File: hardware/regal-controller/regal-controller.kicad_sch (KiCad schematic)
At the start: 23 parts, among them J1 Raspberry_Pi_2_3, J2 Barrel_Jack_Switch_Pin3Ring, J3 Conn_02x05_Odd_Even, J4 Conn_01x02_Male, J5 Conn_01x02_Male, U1 SN65HVD230, U2 MCP2515, Y1 8MHz

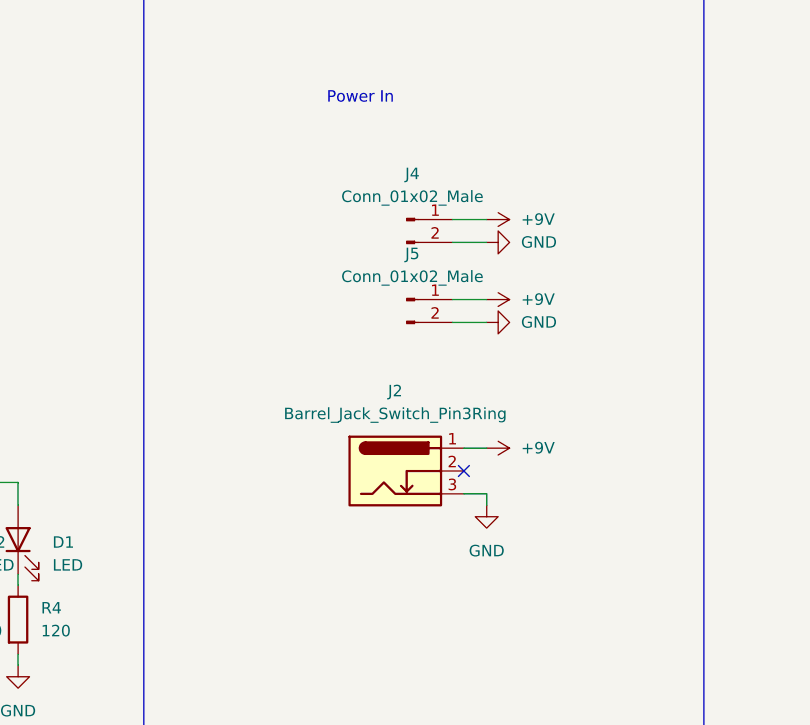
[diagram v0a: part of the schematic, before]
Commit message: 40pol connector rotated and other small mods.
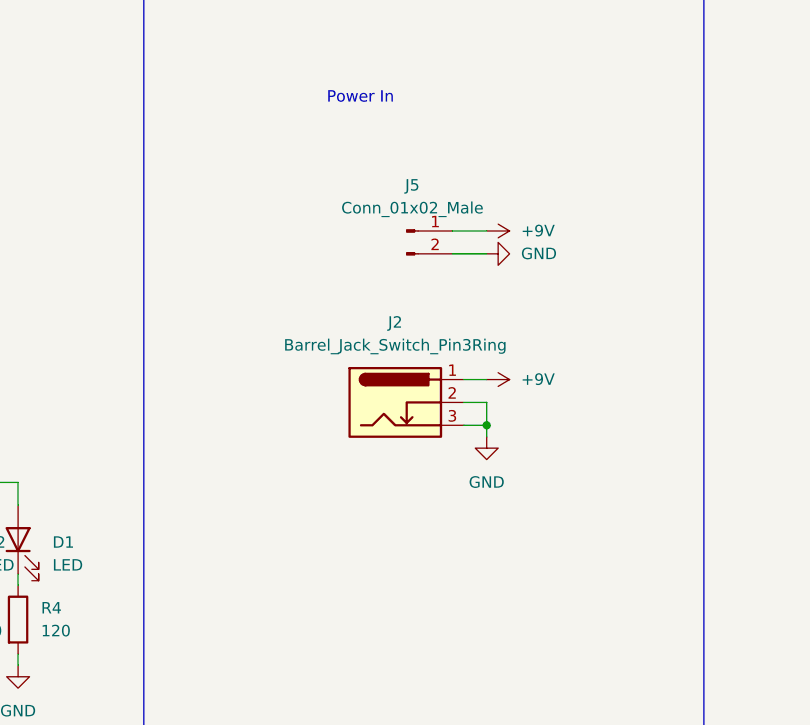
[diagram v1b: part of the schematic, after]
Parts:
- removed J4: Conn_01x02_Male, Connector_JST:JST_VH_B2PS-VH_1x02_P3.96mm_Horizontal, symbol Connector:Conn_01x02_Male
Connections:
- net GND: now also J2.2
- no-connect marks 36 -> 35
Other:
- moved on the sheet: J2, J5

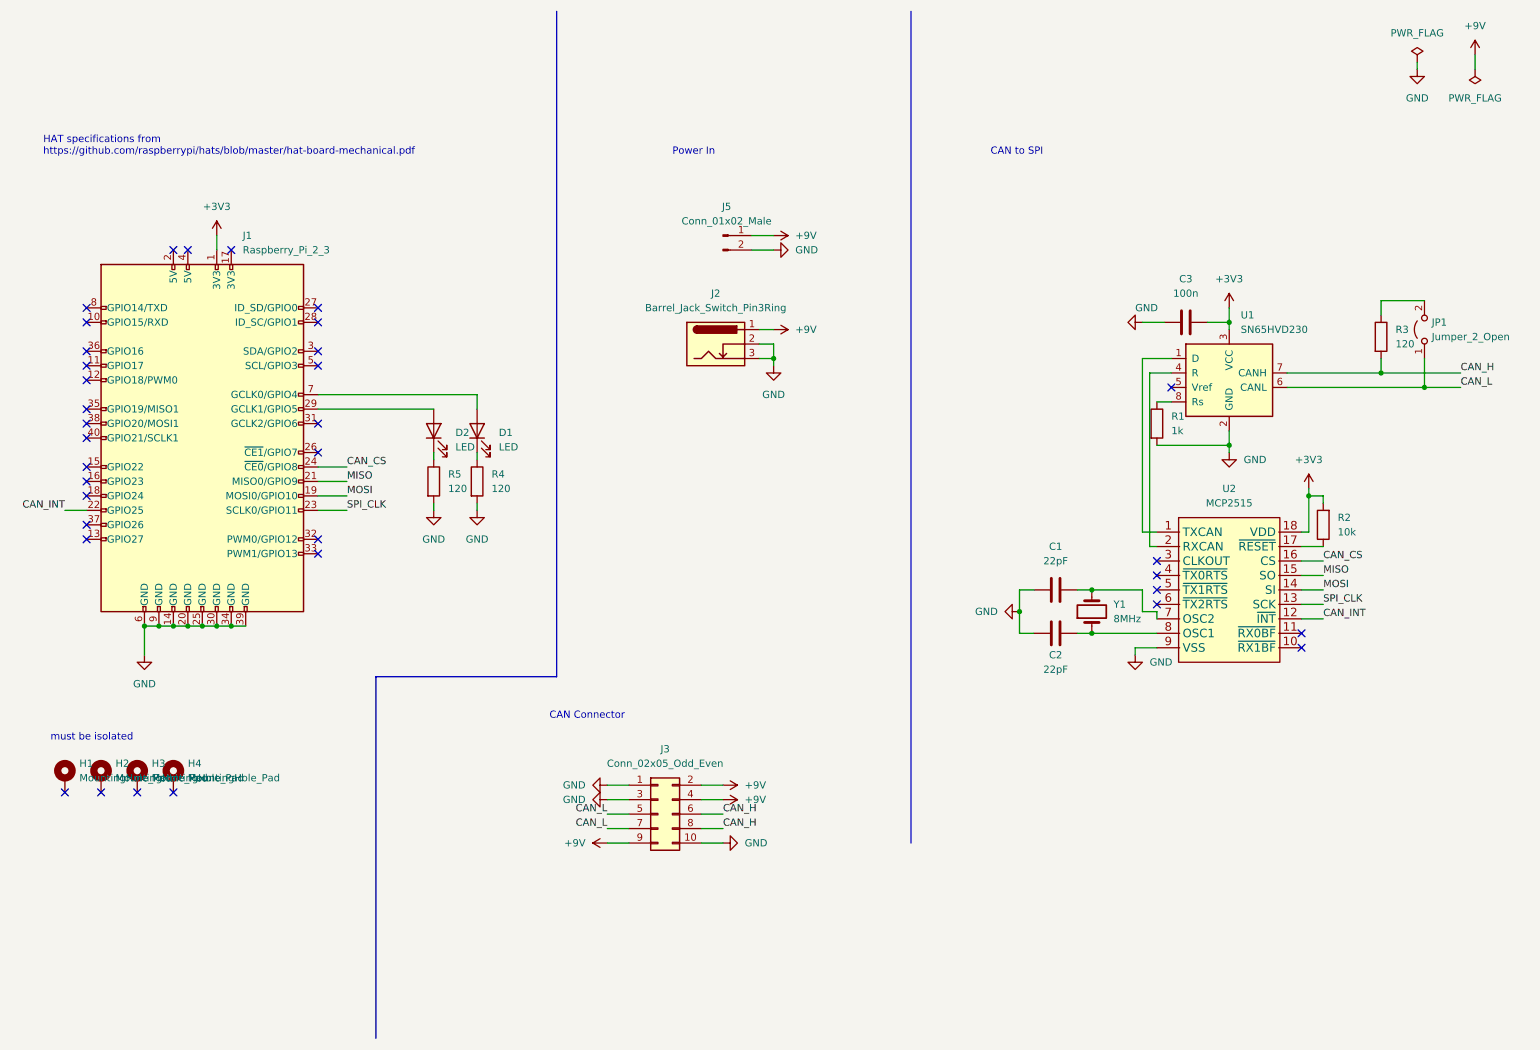
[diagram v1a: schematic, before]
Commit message: shelf controller USB added
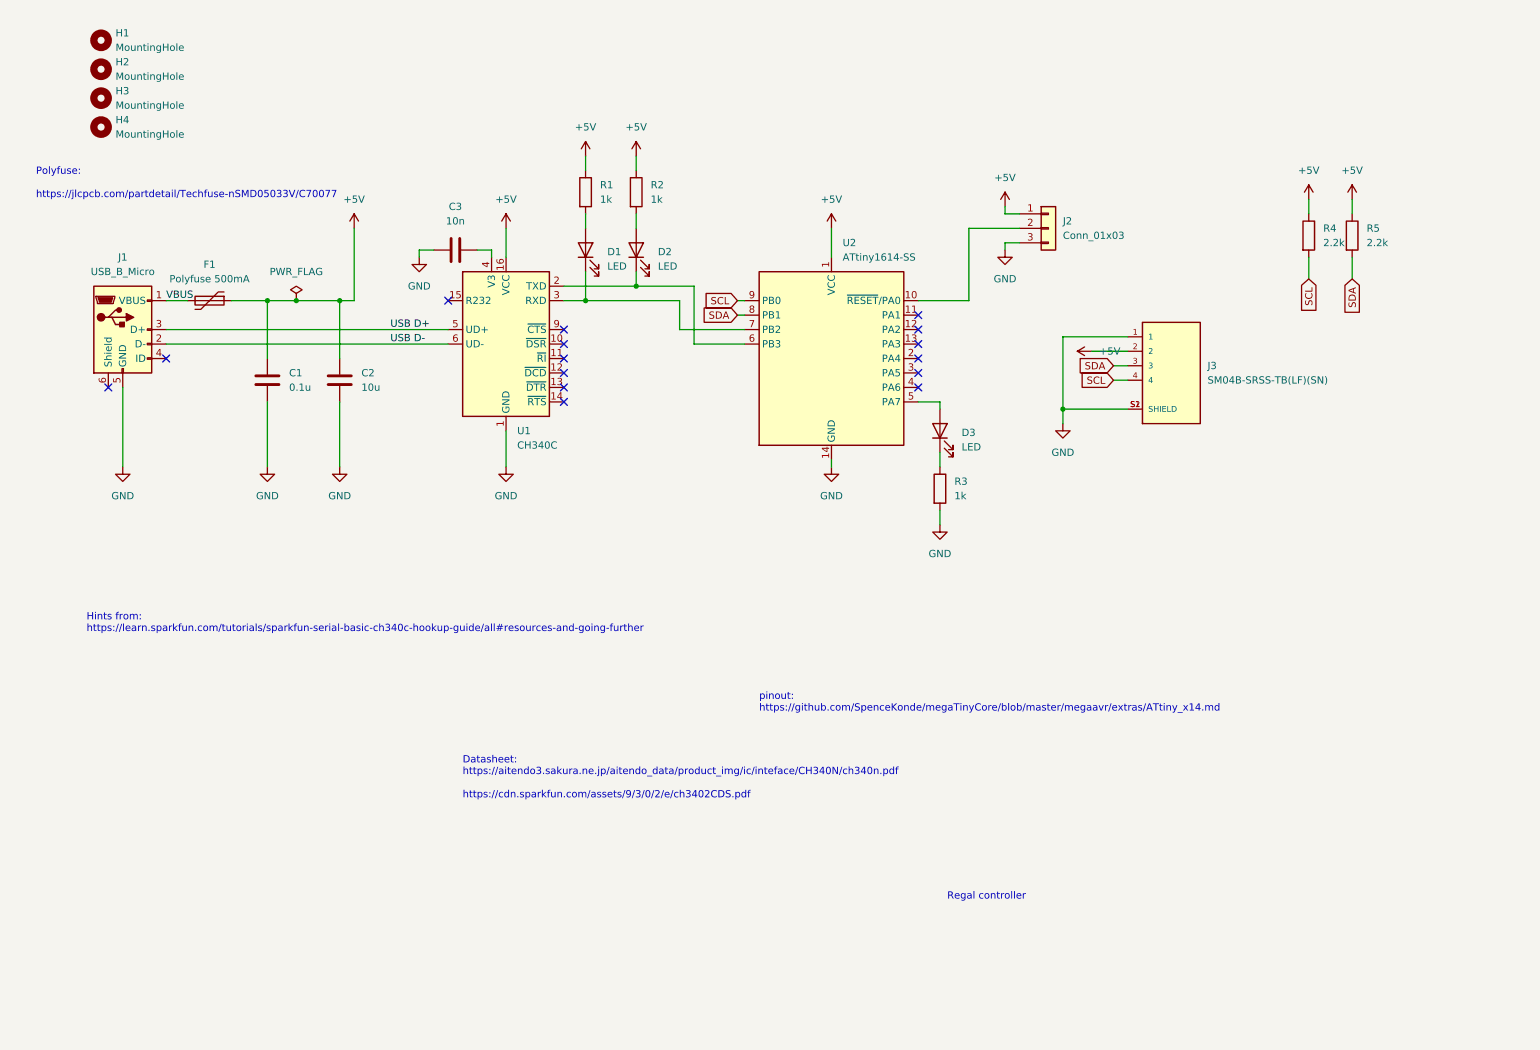
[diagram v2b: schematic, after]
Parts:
- removed H1, H2, H3, H4: MountingHole_Pad, MountingHole:MountingHole_2.7mm_M2.5_Pad_TopBottom, symbol Mechanical:MountingHole_Pad
- removed J1: Raspberry_Pi_2_3, Connector_PinSocket_2.54mm:PinSocket_2x20_P2.54mm_Vertical, symbol Connector:Raspberry_Pi_2_3
- removed J2: Barrel_Jack_Switch_Pin3Ring, Connector_BarrelJack:BarrelJack_Horizontal, symbol Connector:Barrel_Jack_Switch_Pin3Ring
- removed J3: Conn_02x05_Odd_Even, Connector_PinSocket_2.54mm:PinSocket_2x05_P2.54mm_Horizontal, symbol Connector_Generic:Conn_02x05_Odd_Even
- removed J5: Conn_01x02_Male, Connector_PinHeader_2.54mm:PinHeader_1x02_P2.54mm_Vertical, symbol Connector:Conn_01x02_Male
- removed JP1: Jumper_2_Open, TestPoint:TestPoint_2Pads_Pitch2.54mm_Drill0.8mm, symbol Jumper:Jumper_2_Open
- removed U1: SN65HVD230, Package_SO:SOIC-8_3.9x4.9mm_P1.27mm, symbol Interface_CAN_LIN:SN65HVD230
- removed U2: MCP2515, Package_DIP:DIP-18_W7.62mm_LongPads, symbol MCP2515:MCP2515
- removed Y1: 8MHz, Crystal:Crystal_SMD_HC49-SD_HandSoldering, symbol Device:Crystal
- added D3: LED, LED_SMD:LED_1206_3216Metric, symbol Device:LED
- added F1: Polyfuse 500mA, Fuse:Fuse_1206_3216Metric, symbol Device:Polyfuse
- added H1, H2, H3, H4: MountingHole, MountingHole:MountingHole_3.2mm_M3, symbol Mechanical:MountingHole
- added J1: USB_B_Micro, Connector_USB:USB_Micro-B_XKB_U254-051T-4BH83-F1S, symbol Connector:USB_B_Micro
- added J2: Conn_01x03, Connector_PinSocket_2.54mm:PinSocket_1x03_P2.54mm_Vertical, symbol Connector_Generic:Conn_01x03
- added J3: SM04B-SRSS-TB(LF)(SN), MyConnector:JST_SM04B-SRSS-TB(LF)(SN), symbol MyConnector:SM04B-SRSS-TB(LF)(SN)
- added U1: CH340C, Package_SO:SOIC-16_3.9x9.9mm_P1.27mm, symbol Interface_USB:CH340C
- added U2: ATtiny1614-SS, Package_SO:SOIC-14_3.9x8.7mm_P1.27mm, symbol MCU_Microchip_ATtiny:ATtiny1614-SS
- C1: value 22pF -> 0.1u; footprint Capacitor_SMD:C_1206_3216Metric_Pad1.33x1.80mm_HandSolder -> Capacitor_SMD:C_1206_3216Metric
- C2: value 22pF -> 10u; footprint Capacitor_SMD:C_1206_3216Metric_Pad1.33x1.80mm_HandSolder -> Capacitor_SMD:C_1206_3216Metric
- C3: value 100n -> 10n; footprint Capacitor_SMD:C_1206_3216Metric_Pad1.33x1.80mm_HandSolder -> Capacitor_SMD:C_1206_3216Metric
- D1, D2: footprint LED_SMD:LED_1206_3216Metric_Pad1.42x1.75mm_HandSolder -> LED_SMD:LED_1206_3216Metric
- R1: footprint Resistor_SMD:R_1206_3216Metric_Pad1.30x1.75mm_HandSolder -> Resistor_SMD:R_1206_3216Metric
- R2: value 10k -> 1k; footprint Resistor_SMD:R_1206_3216Metric_Pad1.30x1.75mm_HandSolder -> Resistor_SMD:R_1206_3216Metric
- R3: value 120 -> 1k; footprint Resistor_SMD:R_1206_3216Metric_Pad1.30x1.75mm_HandSolder -> Resistor_SMD:R_1206_3216Metric
- R4, R5: value 120 -> 2.2k; footprint Resistor_SMD:R_1206_3216Metric_Pad1.30x1.75mm_HandSolder -> Resistor_SMD:R_1206_3216Metric
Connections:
- net CAN_H is gone; now on net GND: R3.2
- net GND: now also C1.2, C2.2, J1.5 (GND), J2.3 (Pin_3), J3.1, J3.S1 (SHIELD), J3.S2 (SHIELD), U1.1 (GND), U2.14 (GND); no longer C1.1, C2.1, R1.2, R4.2, R5.2
- net +5V: now reaches R1.1
- net +5V: now also C1.1, C2.1, R2.1, R4.1, R5.1, F1.1, J2.1 (Pin_1), J3.2, U1.16 (VCC), U2.1 (VCC)
- net at D2.2 (A): now also R2.2
- net at D1.2 (A): now also R1.2
- net at D2.1 (K): now also U1.2 (TXD), U2.6 (PB3); no longer R5.1
- net at D1.1 (K): now also U1.3 (RXD), U2.7 (PB2); no longer R4.1
- net at R3.1: now also D3.1 (K)
- net +3V3: no longer names the net of C3.2
- net +3V3: now also U1.4 (V3); no longer R2.2
- new net: J2.2 (Pin_2), U2.10 (~{RESET}/PA0)
- new net: D3.2 (A), U2.5 (PA7)
- new net SCL: J3.4, R4.2, U2.9 (PB0)
- new net SDA: J3.3, R5.2, U2.8 (PB1)
- new net USB D+: J1.3 (D+), U1.5 (UD+)
- new net USB D-: J1.2 (D-), U1.6 (UD-)
- new net VBUS: F1.2, J1.1 (VBUS)
- no-connect marks 35 -> 15
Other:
- note added: "Datasheet: https://aitendo3.sakura.ne.jp/aitendo_data/product_img/ic/inteface/CH340N/ch340n.pdf https://cdn.sparkfun.com/assets/9/3/0/2/e/ch3402CDS.pdf"
- note added: "Hints from: https://learn.sparkfun.com/tutorials/sparkfun-serial-basic-ch340c-hookup-guide/all#resources-and-going-further"
- note added: "Polyfuse: https://jlcpcb.com/partdetail/Techfuse-nSMD05033V/C70077"
- note added: "Regal controller"
- note added: "pinout: https://github.com/SpenceKonde/megaTinyCore/blob/master/megaavr/extras/ATtiny_x14.md"
- note removed: "CAN Connector"
- note removed: "CAN to SPI"
- note removed: "HAT specifications from https://github.com/raspberrypi/hats/blob/master/hat-board-mechanical.pdf"
- note removed: "Power In"
- note removed: "must be isolated"
